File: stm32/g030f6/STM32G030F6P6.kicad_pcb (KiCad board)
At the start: 2 copper layers, 17.8 x 25.4 mm, 18 parts, among them J1 STLINK, J2 LEFT, J3 RIGHT, U1 XC6220B331MR, U2 STM32G030F6Px

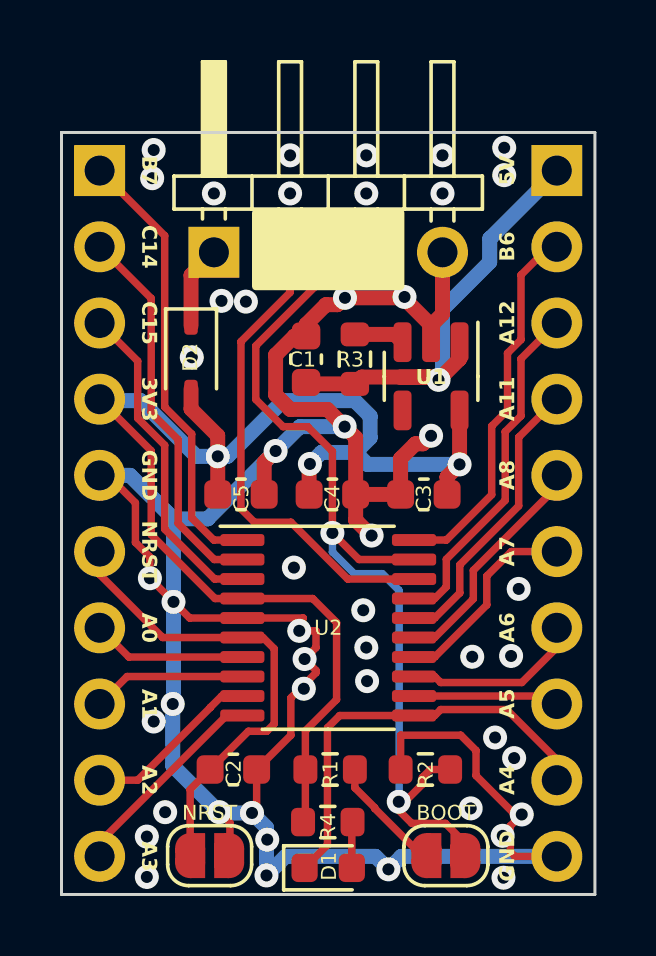
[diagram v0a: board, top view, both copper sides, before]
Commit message: Fix: Diode direction corrected.
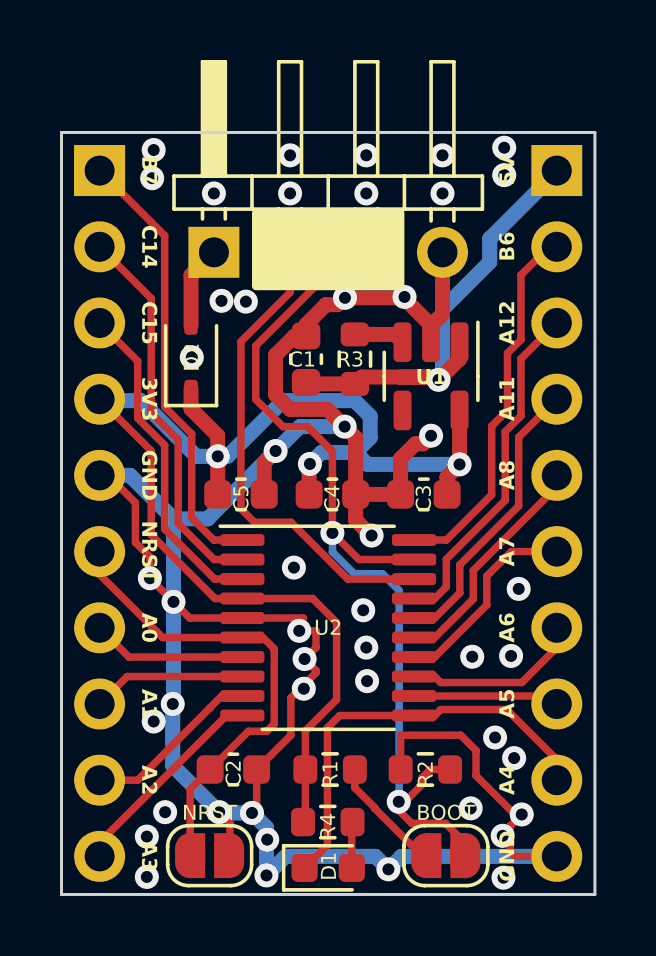
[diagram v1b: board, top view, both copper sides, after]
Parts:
- turned D2 to 90 degrees
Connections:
- D2 pad 1: Net-(D2-K) -> +3.3V
- D2 pad 2: +3.3V -> Net-(D2-A)
- J1 pad 1: Net-(D2-K) -> Net-(D2-A)
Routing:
- net Net-(D2-K): track 2.76 -> 0.00 mm
- net Net-(D2-A): track 0.00 -> 2.76 mm
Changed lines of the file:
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@@
   (net 3 "NRST")
   (net 4 "PA4")
-  (net 5 "Net-(D2-K)")
+  (net 5 "Net-(D2-A)")
   (net 6 "SWDIO")
   (net 7 "SWCLK{slash}BOOT0")
@@
   )
   (footprint "Diode_SMD:D_SOD-323" (layer "F.Cu")
-    (at 77.978 109.093 -90)
+    (at 77.978 109.093 90)
     (descr "SOD-323")
     (tags "SOD-323")
@@
     (fp_line (start 0.9 0.7) (end -0.9 0.7)
       (stroke (width 0.1) (type solid)) (layer "F.Fab"))
-    (pad "1" smd roundrect (at -1.05 0 270) (size 0.6 0.45) (layers "F.Cu" "F.Paste" "F.Mask") (roundrect_rratio 0.25)
-      (net 5 "Net-(D2-K)") (pinfunction "K") (pintype "passive"))
-    (pad "2" smd roundrect (at 1.05 0 270) (size 0.6 0.45) (layers "F.Cu" "F.Paste" "F.Mask") (roundrect_rratio 0.25)
-      (net 2 "+3.3V") (pinfunction "A") (pintype "passive"))
+    (pad "1" smd roundrect (at -1.05 0 90) (size 0.6 0.45) (layers "F.Cu" "F.Paste" "F.Mask") (roundrect_rratio 0.25)
+      (net 2 "+3.3V") (pinfunction "K") (pintype "passive"))
+    (pad "2" smd roundrect (at 1.05 0 90) (size 0.6 0.45) (layers "F.Cu" "F.Paste" "F.Mask") (roundrect_rratio 0.25)
+      (net 5 "Net-(D2-A)") (pinfunction "A") (pintype "passive"))
     (model "${KICAD6_3DMODEL_DIR}/Diode_SMD.3dshapes/D_SOD-323.wrl"
       (offset (xyz 0 0 0))
@@
       (stroke (width 0.1) (type solid)) (layer "F.Fab"))
     (pad "1" thru_hole rect (at 0 0 90) (size 1.7 1.7) (drill 1) (layers "*.Cu" "*.Mask")
-      (net 5 "Net-(D2-K)") (pinfunction "Pin_1") (pintype "passive"))
+      (net 5 "Net-(D2-A)") (pinfunction "Pin_1") (pintype "passive"))
     (pad "2" thru_hole oval (at 0 2.54 90) (size 1.7 1.7) (drill 1) (layers "*.Cu" "*.Mask")
       (net 6 "SWDIO") (pinfunction "Pin_2") (pintype "passive"))

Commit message: WIP: F070F6P6, Fix: Diode direction corrected for F042F6P6.
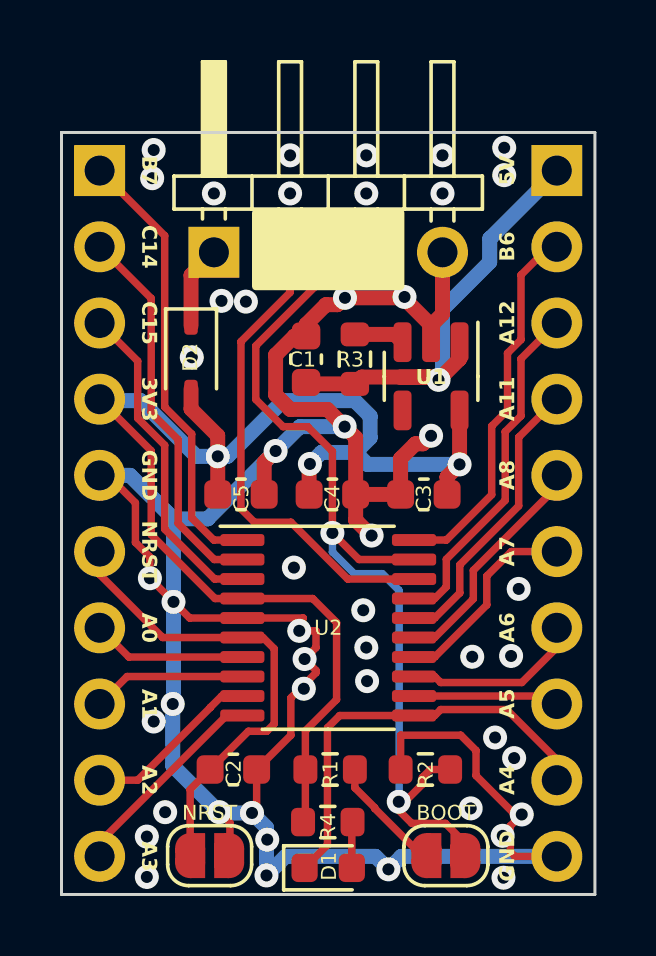
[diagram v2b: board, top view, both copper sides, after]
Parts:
- turned D2 to -90 degrees
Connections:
- D2 pad 1: +3.3V -> Net-(D2-K)
- D2 pad 2: Net-(D2-A) -> +3.3V
- J1 pad 1: Net-(D2-A) -> Net-(D2-K)
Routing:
- net Net-(D2-K): track 0.00 -> 2.76 mm
- net Net-(D2-A): track 2.76 -> 0.00 mm
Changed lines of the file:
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@@
   (net 3 "NRST")
   (net 4 "PA4")
-  (net 5 "Net-(D2-A)")
+  (net 5 "Net-(D2-K)")
   (net 6 "SWDIO")
   (net 7 "SWCLK{slash}BOOT0")
@@
   )
   (footprint "Diode_SMD:D_SOD-323" (layer "F.Cu")
-    (at 77.978 109.093 90)
+    (at 77.978 109.093 -90)
     (descr "SOD-323")
     (tags "SOD-323")
@@
     (fp_line (start 0.9 0.7) (end -0.9 0.7)
       (stroke (width 0.1) (type solid)) (layer "F.Fab"))
-    (pad "1" smd roundrect (at -1.05 0 90) (size 0.6 0.45) (layers "F.Cu" "F.Paste" "F.Mask") (roundrect_rratio 0.25)
-      (net 2 "+3.3V") (pinfunction "K") (pintype "passive"))
-    (pad "2" smd roundrect (at 1.05 0 90) (size 0.6 0.45) (layers "F.Cu" "F.Paste" "F.Mask") (roundrect_rratio 0.25)
-      (net 5 "Net-(D2-A)") (pinfunction "A") (pintype "passive"))
+    (pad "1" smd roundrect (at -1.05 0 270) (size 0.6 0.45) (layers "F.Cu" "F.Paste" "F.Mask") (roundrect_rratio 0.25)
+      (net 5 "Net-(D2-K)") (pinfunction "K") (pintype "passive"))
+    (pad "2" smd roundrect (at 1.05 0 270) (size 0.6 0.45) (layers "F.Cu" "F.Paste" "F.Mask") (roundrect_rratio 0.25)
+      (net 2 "+3.3V") (pinfunction "A") (pintype "passive"))
     (model "${KICAD6_3DMODEL_DIR}/Diode_SMD.3dshapes/D_SOD-323.wrl"
       (offset (xyz 0 0 0))
@@
       (stroke (width 0.1) (type solid)) (layer "F.Fab"))
     (pad "1" thru_hole rect (at 0 0 90) (size 1.7 1.7) (drill 1) (layers "*.Cu" "*.Mask")
-      (net 5 "Net-(D2-A)") (pinfunction "Pin_1") (pintype "passive"))
+      (net 5 "Net-(D2-K)") (pinfunction "Pin_1") (pintype "passive"))
     (pad "2" thru_hole oval (at 0 2.54 90) (size 1.7 1.7) (drill 1) (layers "*.Cu" "*.Mask")
       (net 6 "SWDIO") (pinfunction "Pin_2") (pintype "passive"))
